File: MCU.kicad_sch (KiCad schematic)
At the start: 45 parts, among them J15 Conn_01x08, J16 Conn_02x04_Odd_Even, J17 TFC-103-01-F-D, J19 TFC-103-01-F-D, Q13 SI2300, SW1 SW_Push_Dual, SW2 SW_Push_Dual, SW3 SW_DIP_x08, U15 MCP1700-3302E_SOT23, U16 CD74HC4067M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

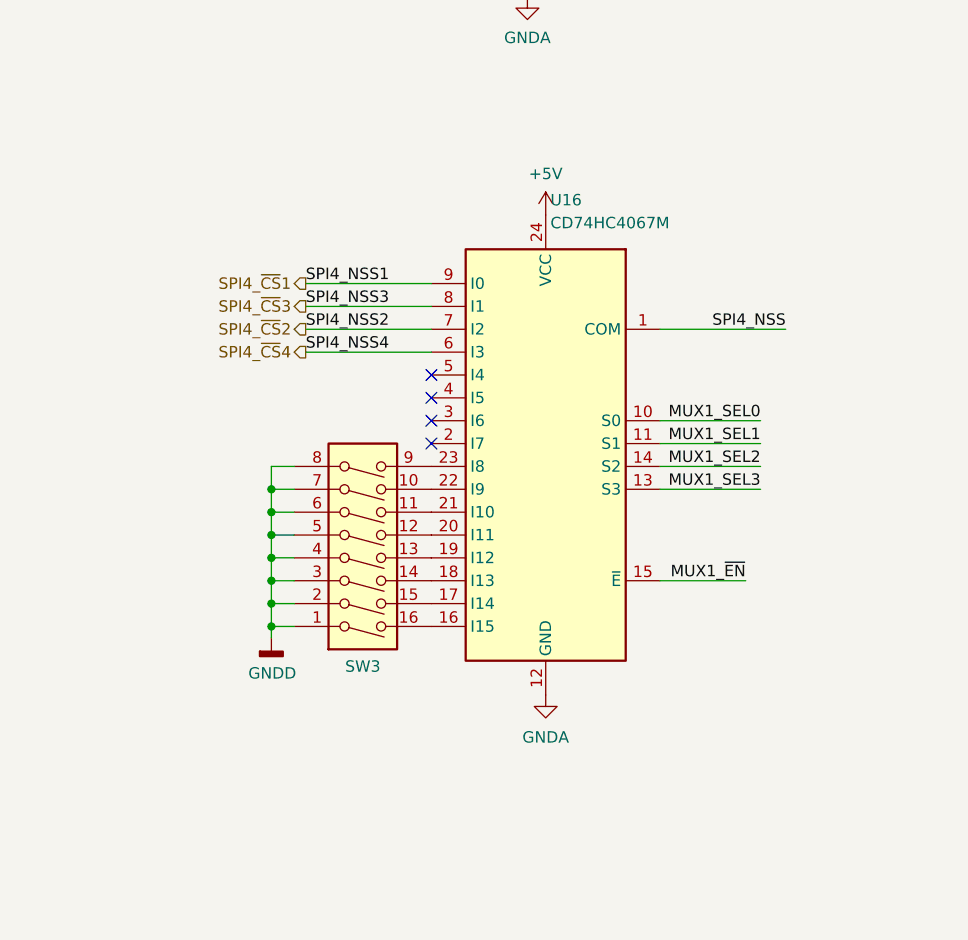
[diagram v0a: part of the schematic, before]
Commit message: Added 2nd SPI4 connector
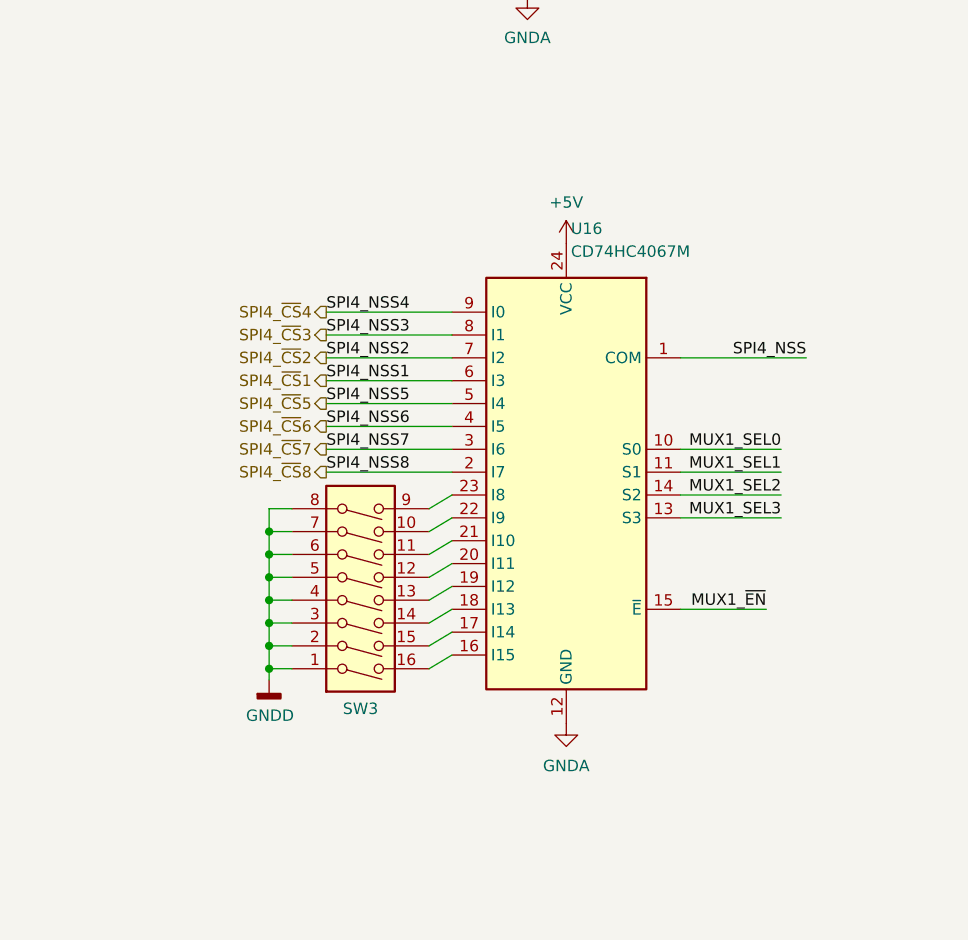
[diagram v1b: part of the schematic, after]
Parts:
- J17, J19: footprint SAMTEC_TFC-103-01-F-D -> (none)
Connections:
- net SPI4_~{CS}1: now also U16.6 (I3); no longer U16.9 (I0)
- net SPI4_~{CS}4: now also U16.9 (I0); no longer U16.6 (I3)
- net SPI4_~{CS}8: now reaches U16.2 (I7)
- net SPI4_~{CS}7: now reaches U16.3 (I6)
- net SPI4_~{CS}6: now reaches U16.4 (I5)
- net SPI4_~{CS}5: now reaches U16.5 (I4)
- no-connect marks 17 -> 13
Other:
- moved on the sheet: SW3, U16

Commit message: Ready for first review
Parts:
- J17, J19: footprint (none) -> TXV_Library_Footprints:SAMTEC_TFC-103-01-F-D
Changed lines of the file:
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@@
     (property "Reference" "J19" (id 0) (at 59.055 207.01 0))
     (property "Value" "TFC-103-01-F-D" (id 1) (at 59.055 209.55 0))
-    (property "Footprint" "" (id 2) (at 59.055 217.17 0)
+    (property "Footprint" "TXV_Library_Footprints:SAMTEC_TFC-103-01-F-D" (id 2) (at 59.055 217.17 0)
       (effects (font (size 1.27 1.27)) (justify bottom) hide)
     )
@@
     (property "Reference" "J17" (id 0) (at 59.055 186.69 0))
     (property "Value" "TFC-103-01-F-D" (id 1) (at 59.055 189.23 0))
-    (property "Footprint" "" (id 2) (at 59.055 196.85 0)
+    (property "Footprint" "TXV_Library_Footprints:SAMTEC_TFC-103-01-F-D" (id 2) (at 59.055 196.85 0)
       (effects (font (size 1.27 1.27)) (justify bottom) hide)
     )

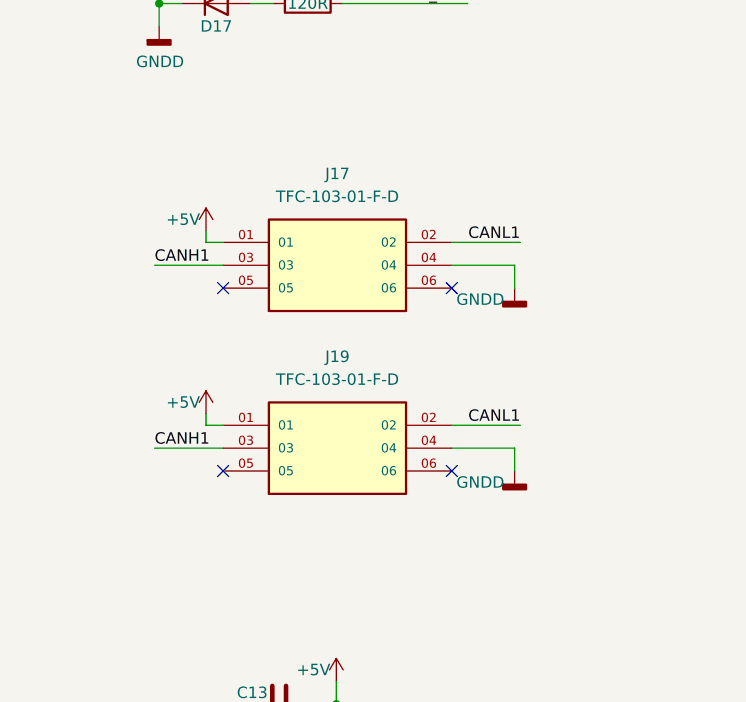
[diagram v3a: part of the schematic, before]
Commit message: Added different Can connector
Used T1M-04-F-SV-L as a can connector
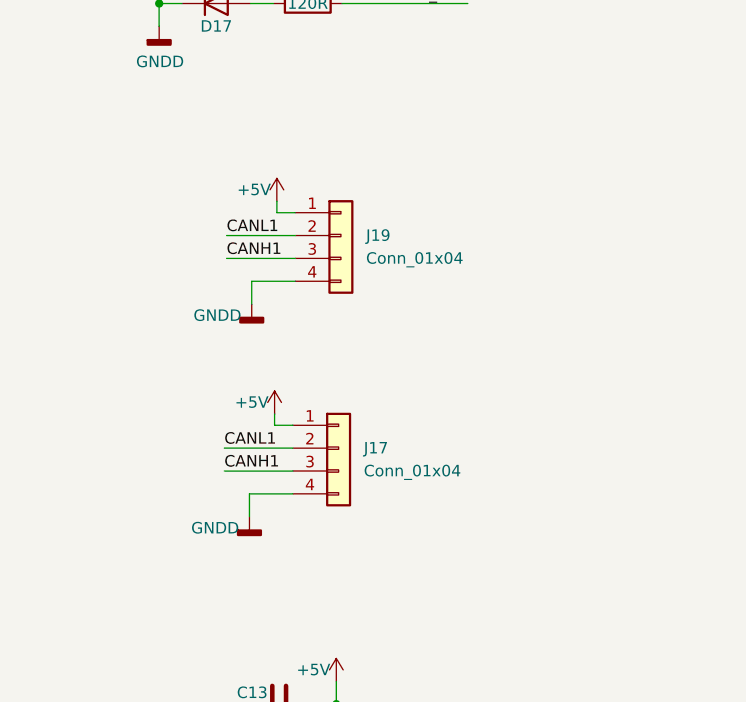
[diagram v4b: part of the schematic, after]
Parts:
- removed J17, J19: TFC-103-01-F-D, TXV_Library_Footprints:SAMTEC_TFC-103-01-F-D, symbol TFC-103-01-F-D:TFC-103-01-F-D
- added J17, J19: Conn_01x04, T1M-04-F-SV-L:SAMTEC_T1M-04-F-SV-L, symbol Connector_Generic:Conn_01x04
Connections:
- net +5V: now also J17.1 (Pin_1), J19.1 (Pin_1)
- net CANH1: now also J17.3 (Pin_3), J19.3 (Pin_3)
- net CANL1: now also J17.2 (Pin_2), J19.2 (Pin_2)
- net GND: now also J17.4 (Pin_4), J19.4 (Pin_4)
- no-connect marks 13 -> 9

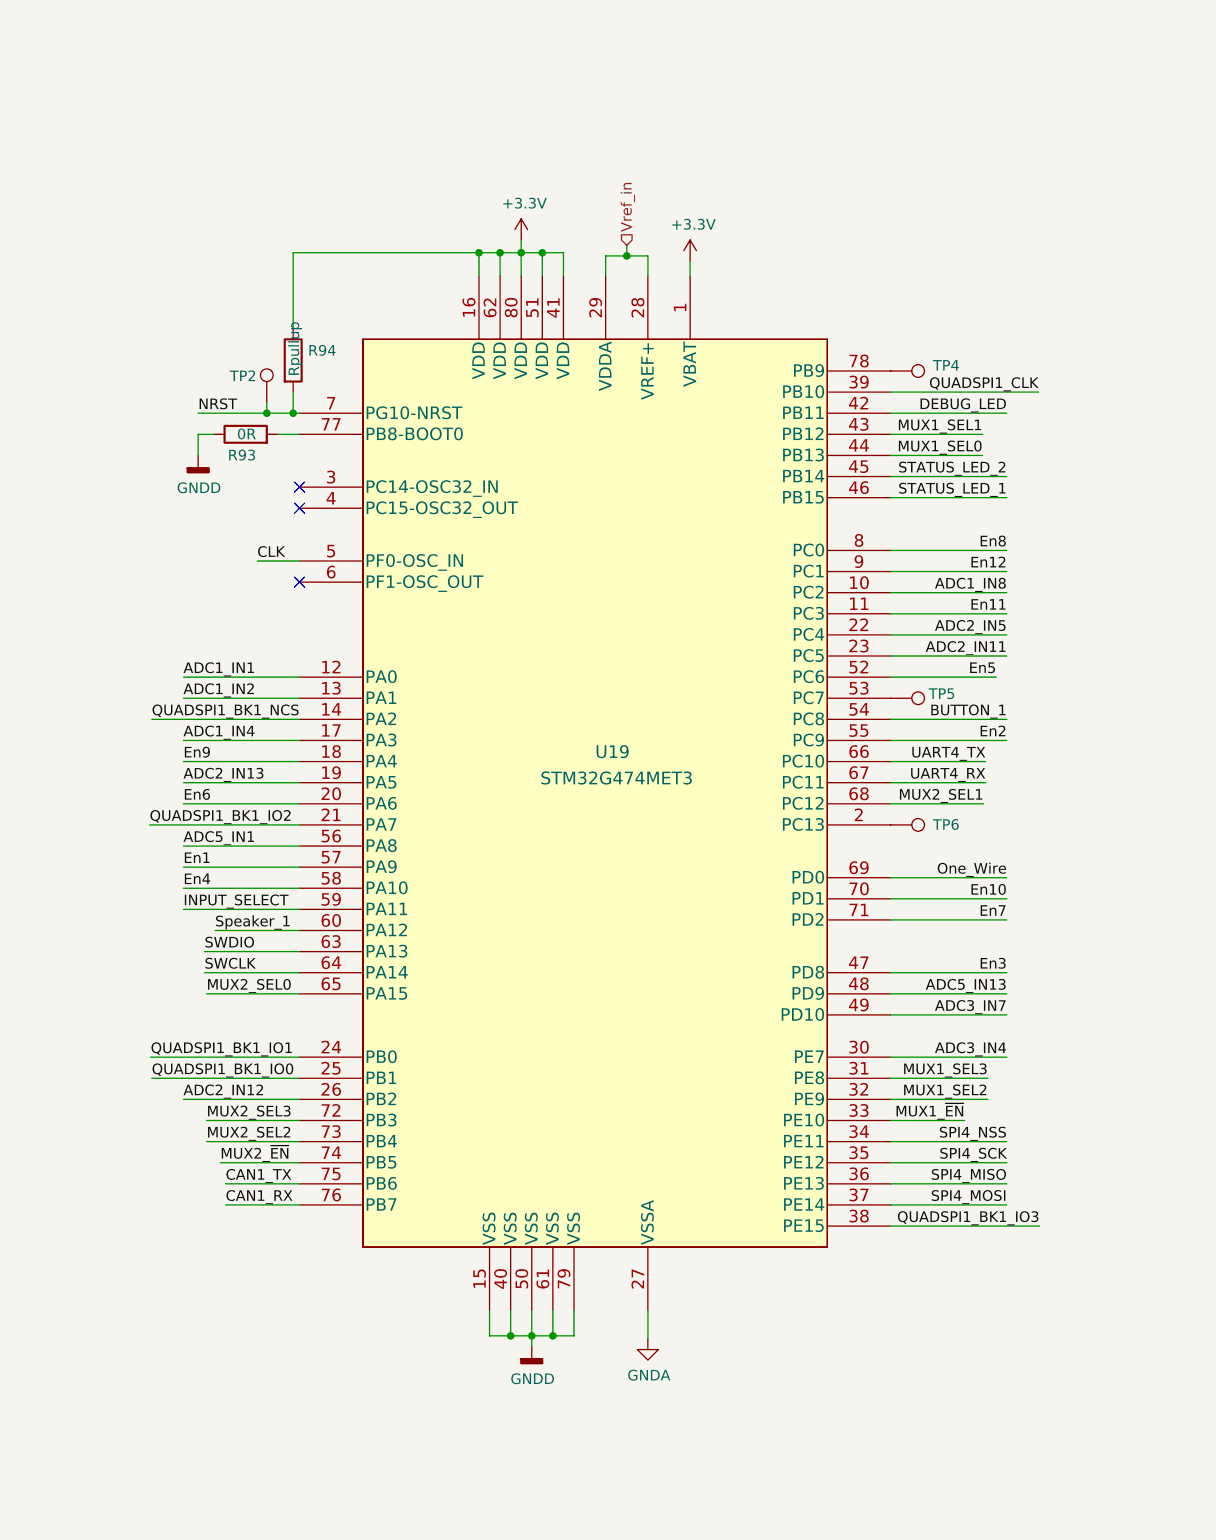
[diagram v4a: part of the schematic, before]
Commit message: Layer change + INA change + SPI 24V added + minor changes
Stitching is still missing
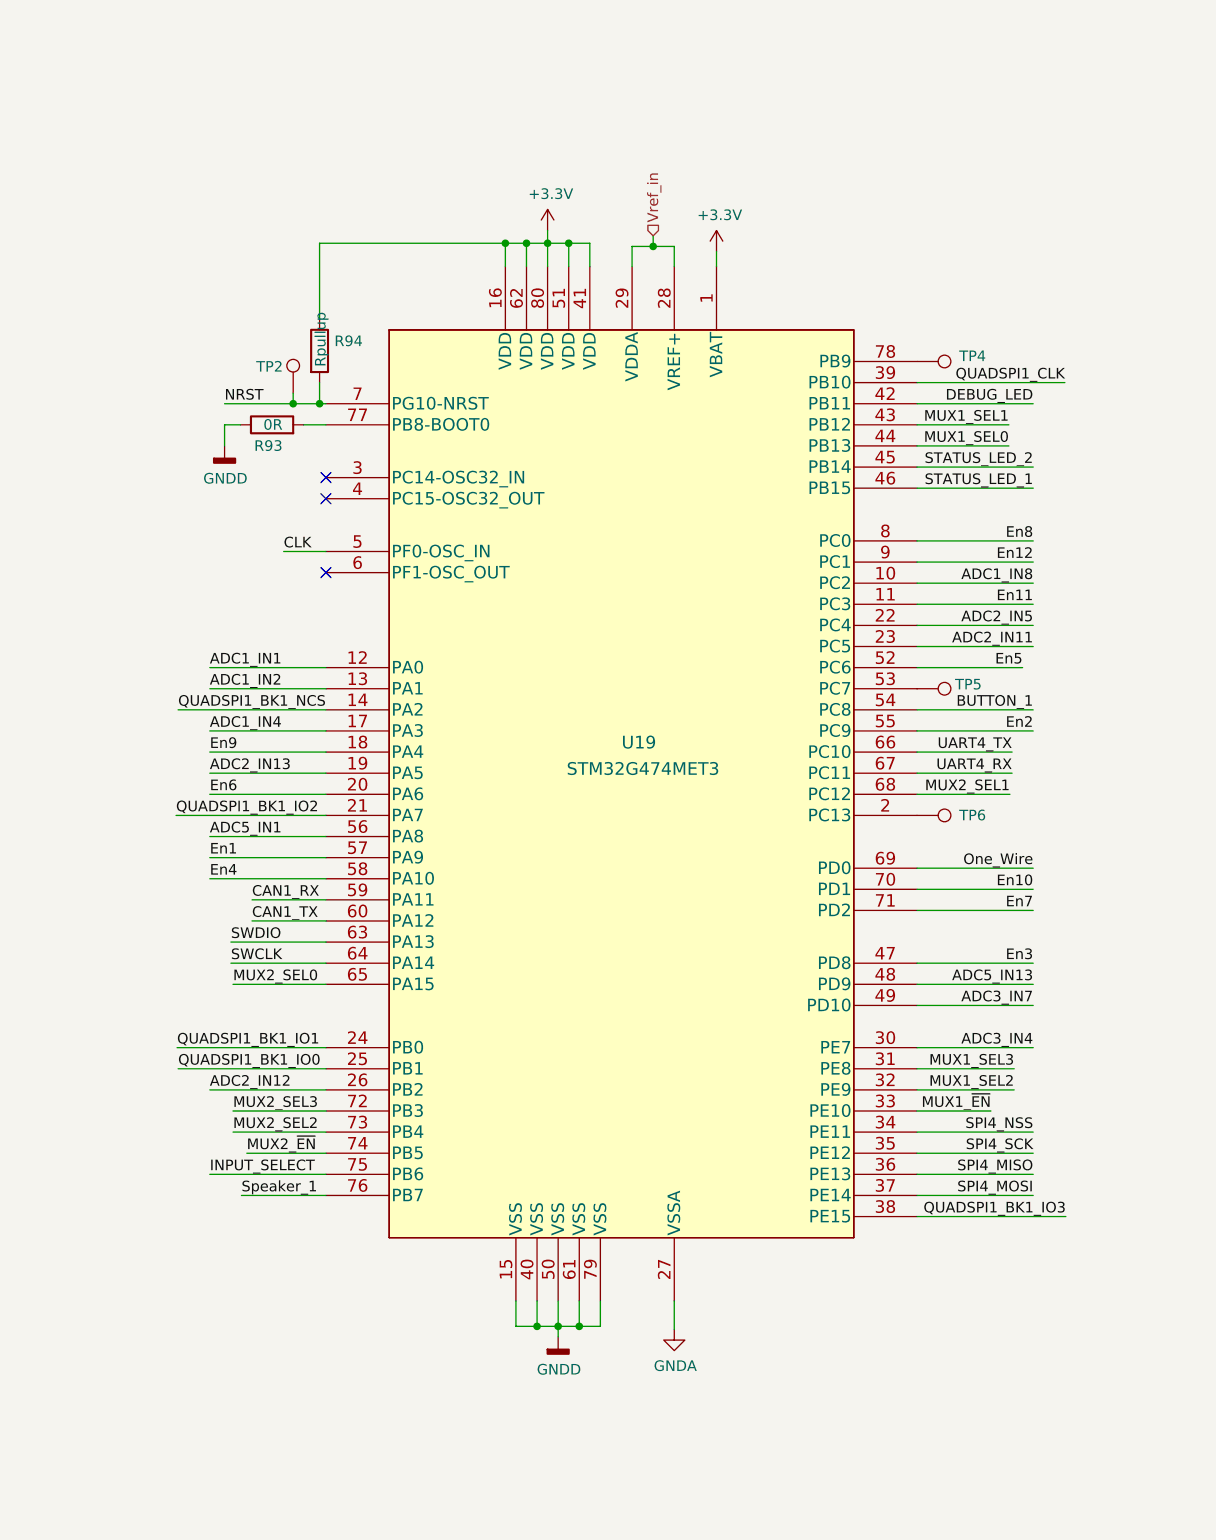
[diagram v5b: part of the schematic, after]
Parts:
- C12, C16, C17, C18, C19, C9: footprint Capacitor_SMD:C_0603_1608Metric -> Capacitor_SMD:C_0402_1005Metric
- J17, J19: footprint T1M-04-F-SV-L:SAMTEC_T1M-04-F-SV-L -> Connector_Molex:Molex_SL_171971-0004_1x04_P2.54mm_Vertical
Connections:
- net CAN1_RX: now also U19.59 (PA11); no longer U19.76 (PB7)
- net CAN1_TX: now also U19.60 (PA12); no longer U19.75 (PB6)
- net INPUT_SELECT: now also U19.75 (PB6); no longer U19.59 (PA11)
- net Speaker_1: now also U19.76 (PB7); no longer U19.60 (PA12)
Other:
- moved on the sheet: R93, R94, TP2, TP4, TP5, TP6, U19

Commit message: All GNDD and GNDA changed to GND
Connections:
- net GNDA is gone; now on net GND: Q13.2 (S), U16.12 (GND), U19.27 (VSSA), U20.12 (GND)

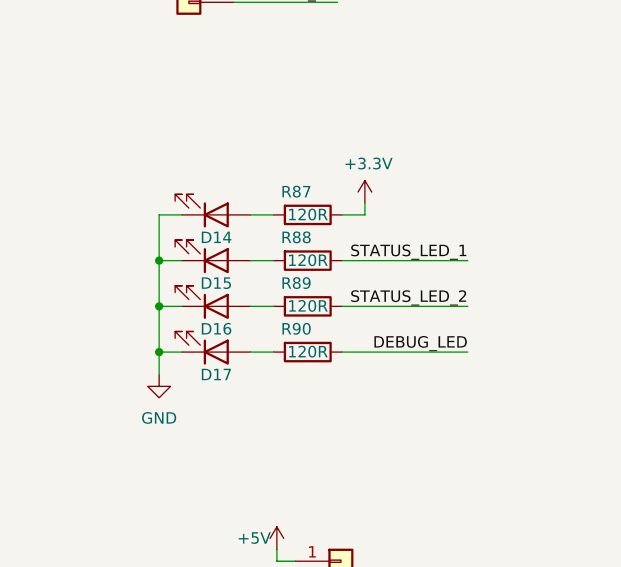
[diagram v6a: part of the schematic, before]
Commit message: Changed 5V Plane to 3.3V Changed INA350 Supply to 3.3V Minor tweaks
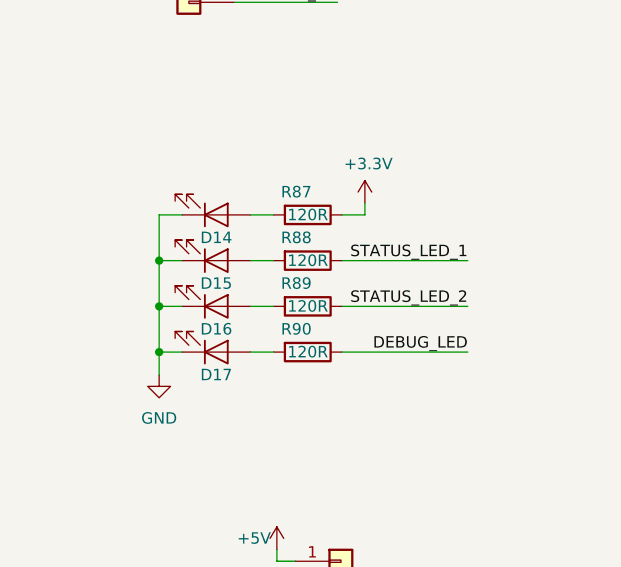
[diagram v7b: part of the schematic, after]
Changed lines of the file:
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@@
     (pin "2")
   )
-  (symbol (lib_id "Device:LED") (at 45.593 167.767 0) (mirror x) (unit 1)
+  (symbol (lib_name "LED_1") (lib_id "Device:LED") (at 45.593 167.767 0) (mirror x) (unit 1)
     (in_bom yes) (on_board yes)
     (property "Reference" "D17" (id 0) (at 45.593 170.307 0))
@@
     (pin "1")
   )
-  (symbol (lib_id "Device:LED") (at 45.593 152.527 0) (mirror x) (unit 1)
+  (symbol (lib_name "LED_3") (lib_id "Device:LED") (at 45.593 152.527 0) (mirror x) (unit 1)
     (in_bom yes) (on_board yes)
     (property "Reference" "D14" (id 0) (at 45.593 155.067 0))
@@
     (pin "9")
   )
-  (symbol (lib_id "Device:LED") (at 45.593 162.687 0) (mirror x) (unit 1)
+  (symbol (lib_name "LED_2") (lib_id "Device:LED") (at 45.593 162.687 0) (mirror x) (unit 1)
     (in_bom yes) (on_board yes)
     (property "Reference" "D16" (id 0) (at 45.593 165.227 0))

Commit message: Fixed Lib Mess
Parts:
- C14: symbol IOB-rescue:CP1-Device -> Device:CP
- U18: symbol IOB-rescue:W25Q256JV-TXV_Library_Symbols -> TXV_Library_Symbols:W25Q256JV
- U19: footprint STM32:STM32G474MET3 -> Package_QFP:LQFP-80_12x12mm_P0.5mm; symbol 2022-11-19_20-38-52:STM32G474MET3 -> TXV_Library_Symbols:STM32G474MET3
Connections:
- no-connect marks 9 -> 10
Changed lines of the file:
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@@
   (junction (at 125.476 207.264) (diameter 0) (color 0 0 0 0)
   )
+  (no_connect (at 128.143 269.875))
   (no_connect (at 47.625 123.825))
   (no_connect (at 245.11 85.852))
@@
     (pin "1")
   )
-  (symbol (lib_id "IOB-rescue:W25Q256JV-TXV_Library_Symbols") (at 135.763 259.715 0) (unit 1)
+  (symbol (lib_id "TXV_Library_Symbols:W25Q256JV") (at 135.763 259.715 0) (unit 1)
     (in_bom yes) (on_board yes)
     (property "Reference" "U18" (id 0) (at 126.873 250.825 0))
@@
     (pin "7")
     (pin "8")
+    (pin "9")
   )
   (symbol (lib_id "power:GND") (at 58.928 274.828 0) (unit 1)
@@
     (pin "1")
   )
-  (symbol (lib_id "IOB-rescue:CP1-Device") (at 76.327 30.099 0) (unit 1)
+  (symbol (lib_id "Device:CP") (at 76.327 30.099 0) (unit 1)
     (in_bom yes) (on_board yes)
     (property "Reference" "C14" (id 0) (at 79.248 28.9306 0)
@@
       (effects (font (size 1.27 1.27)) (justify left))
     )
-    (property "Footprint" "Capacitor_SMD:CP_Elec_6.3x4.9" (id 2) (at 76.327 30.099 0)
+    (property "Footprint" "Capacitor_SMD:CP_Elec_6.3x4.9" (id 2) (at 77.2922 33.909 0)
       (effects (font (size 1.27 1.27)) hide)
     )
@@
     (pin "8")
   )
-  (symbol (lib_id "2022-11-19_20-38-52:STM32G474MET3") (at 245.11 73.152 0) (unit 1)
+  (symbol (lib_id "TXV_Library_Symbols:STM32G474MET3") (at 245.11 73.152 0) (unit 1)
     (in_bom yes) (on_board yes)
     (property "Reference" "U19" (id 0) (at 280.67 117.729 0)
@@
       (effects (font (size 1.524 1.524)) (justify left))
     )
-    (property "Footprint" "STM32:STM32G474MET3" (id 2) (at 280.67 125.222 0)
+    (property "Footprint" "Package_QFP:LQFP-80_12x12mm_P0.5mm" (id 2) (at 280.67 125.222 0)
       (effects (font (size 1.524 1.524)) hide)
     )
